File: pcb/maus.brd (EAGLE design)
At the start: 100 x 100 mm, 97 parts, among them J1 SS-52300-001, Q1 BSS123, Q2 BSS123, Q3 BSS123, Q4 BSS123, Q5 BSS123, Q6 PMN30XPEAHEATSINK, Q7 PMN30XPEAHEATSINK, U1 ESP32-S2-WROOM, U2 CH340C, U4 LP3965EMP-3.3, U5 LSM9DS1TR, U6 LM358DR

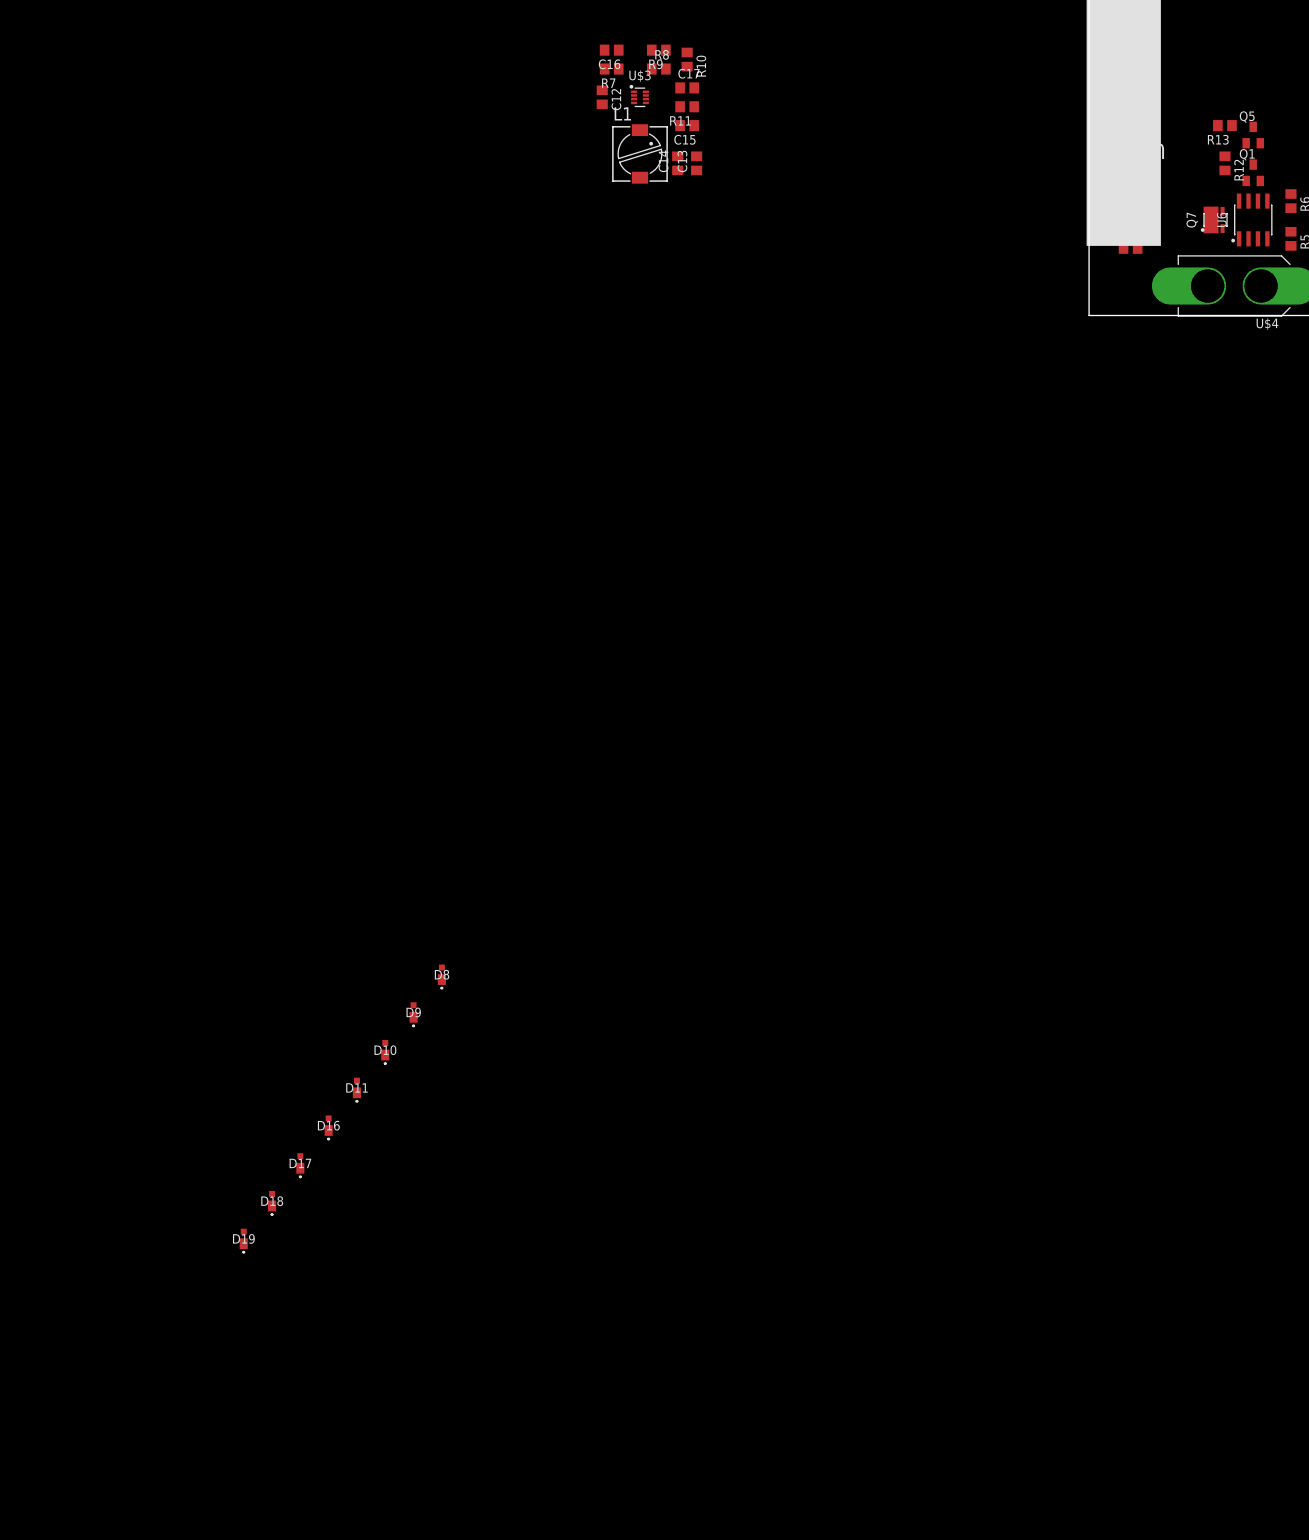
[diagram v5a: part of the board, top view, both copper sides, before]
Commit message: replaced buck converter
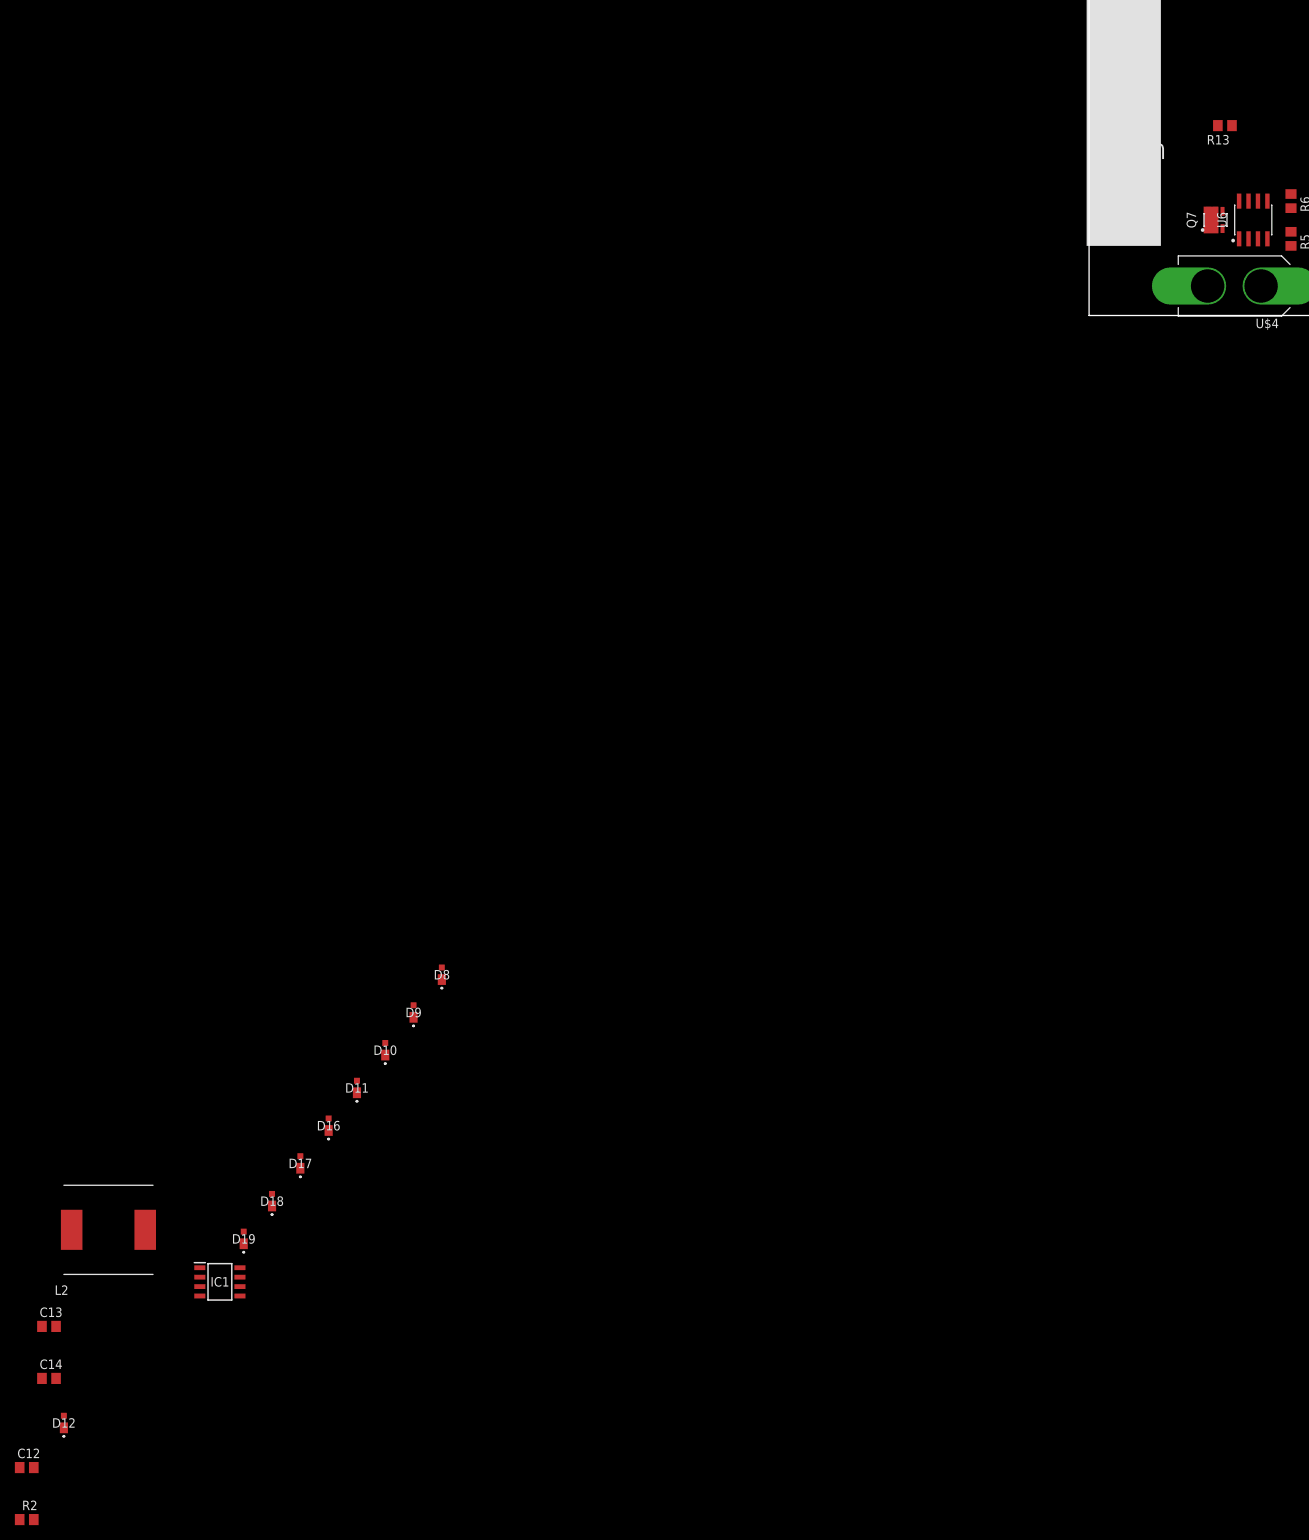
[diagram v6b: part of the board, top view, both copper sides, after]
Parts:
- removed C15: 1u, rcl:C0805
- removed C16, C19: 1n, rcl:C0805
- removed C17: 6.8n, rcl:C0805
- removed L1: 2.2u, rcl:PIS2816
- removed Q1, Q5: BSS123, transistor-small-signal:SOT23
- removed R10: 7.68k, rcl:R0805
- removed R11: 20, rcl:R0805
- removed R12, R7: 22k, rcl:R0805
- removed R14: 470k, rcl:R0805
- removed R15: 100k, rcl:R0805
- removed R8: 10k, rcl:R0805
- removed R9: 40.2k, rcl:R0805
- removed U$3: MP2333HSOT583, MP2333H:SOTFL50P175X60-8N
- added D12: RBR2VWM40ATF, shared:RB068VWM100
- added IC1: AP1509-50SG-13, shared:SOIC127P600X175-8N
- added L2: 744770147, shared:WE-PD_1260/1245/1280/121054
- added R2: 10k, rcl:R0805
- R13: value 22k -> 10k
- moved C12 200.1 mm to (-127.0, -140.0), turned to 0 degrees
- moved C14 184.2 mm to (-124.0, -128.0), turned to 0 degrees
- moved C13 179.2 mm to (-124.0, -121.0), turned to 0 degrees
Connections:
- removed net BUCK_EN: C19.1, R14.1, R15.2, U$3.6
- removed net N$14: C15.2, L1.1, U$3.3
- removed net N$15: R10.2, R8.2, R9.1
- removed net N$16: R8.1, U$3.8
- removed net N$17: R11.2, U$3.5
- removed net N$18: C15.1, R11.1
- removed net N$19: C17.1, U$3.7
- removed net N$20: Q1.3, Q5.1, R12.1
- removed net PGOOD: C16.1, Q1.1, R7.1, U$3.1
- new net N$3: D12.1, IC1.2, L2.1
- net +5V: now also IC1.3, L2.2; no longer L1.2, R9.2
- net /VBUS_EN: no longer R12.2
- net EN_3V3: no longer Q5.3
- net GND: now also D12.2, IC1.5, IC1.6, IC1.7, IC1.8, R2.1; no longer C16.2, C17.2, C19.2, Q1.2, Q5.2, R10.1, R15.1, U$3.4
- net USB_VBUS: now also IC1.4, R2.2
- net VBAT: now also IC1.1; no longer R14.2, R7.2, U$3.2

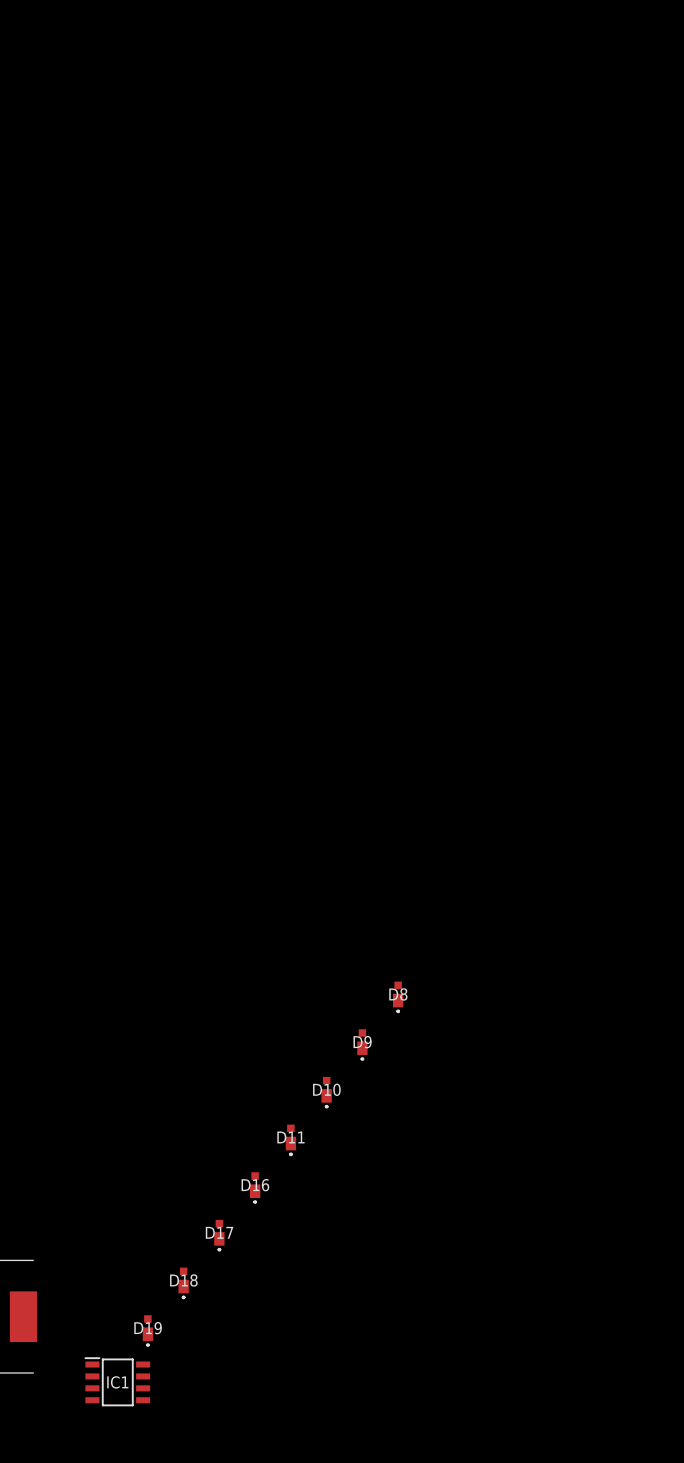
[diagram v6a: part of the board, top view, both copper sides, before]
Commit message: set minimum trach widths
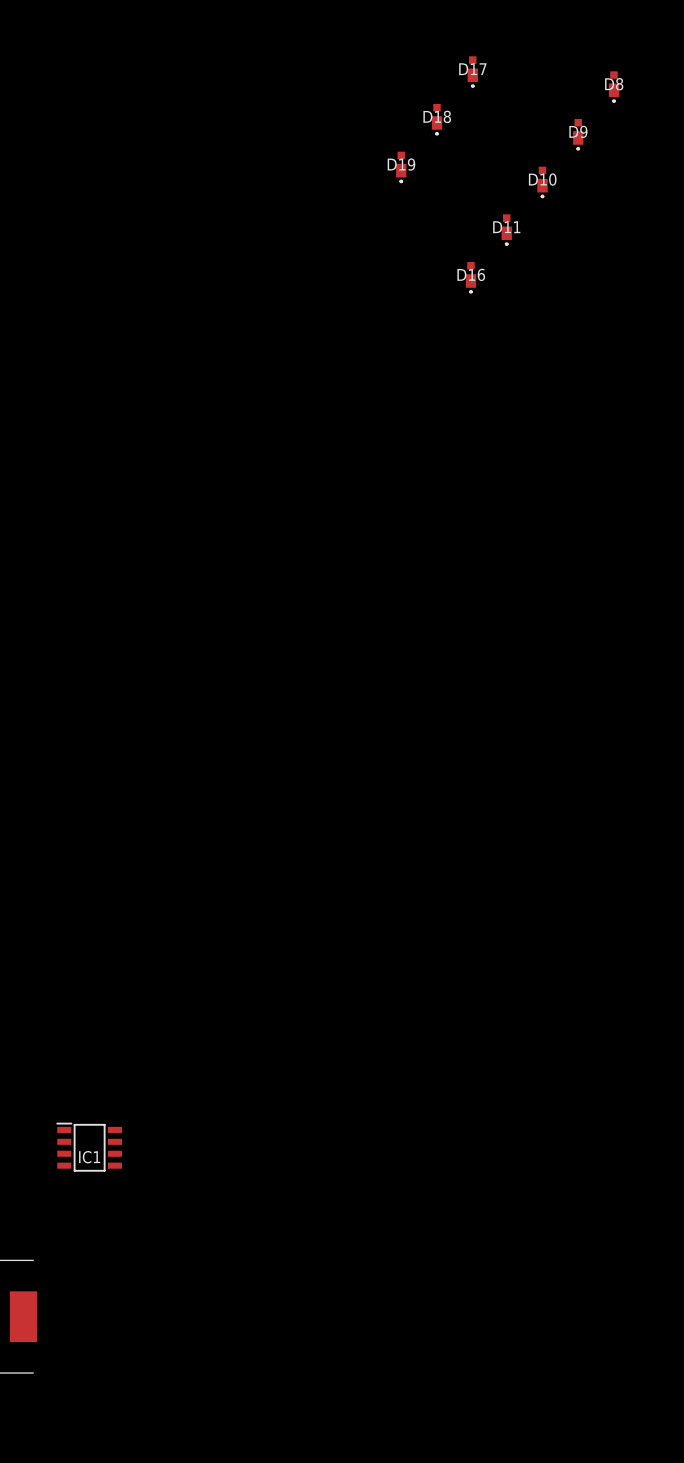
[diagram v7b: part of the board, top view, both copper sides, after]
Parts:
- moved D17 126.9 mm to (-63.2, 24.9)
- moved D18 126.9 mm to (-67.0, 19.9)
- moved D19 126.9 mm to (-70.8, 14.8)
- moved D10 99.7 mm to (-55.7, 13.2)
- moved D11 99.7 mm to (-59.5, 8.10)
- moved D16 99.7 mm to (-63.4, 3.02)
- moved D8 99.7 mm to (-48.1, 23.3)
- moved D9 99.7 mm to (-51.9, 18.3)
- moved IC1 25.2 mm to (-104.0, -90.0)
